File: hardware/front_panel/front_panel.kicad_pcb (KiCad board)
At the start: 2 copper layers, 60 x 40 mm, 4 parts

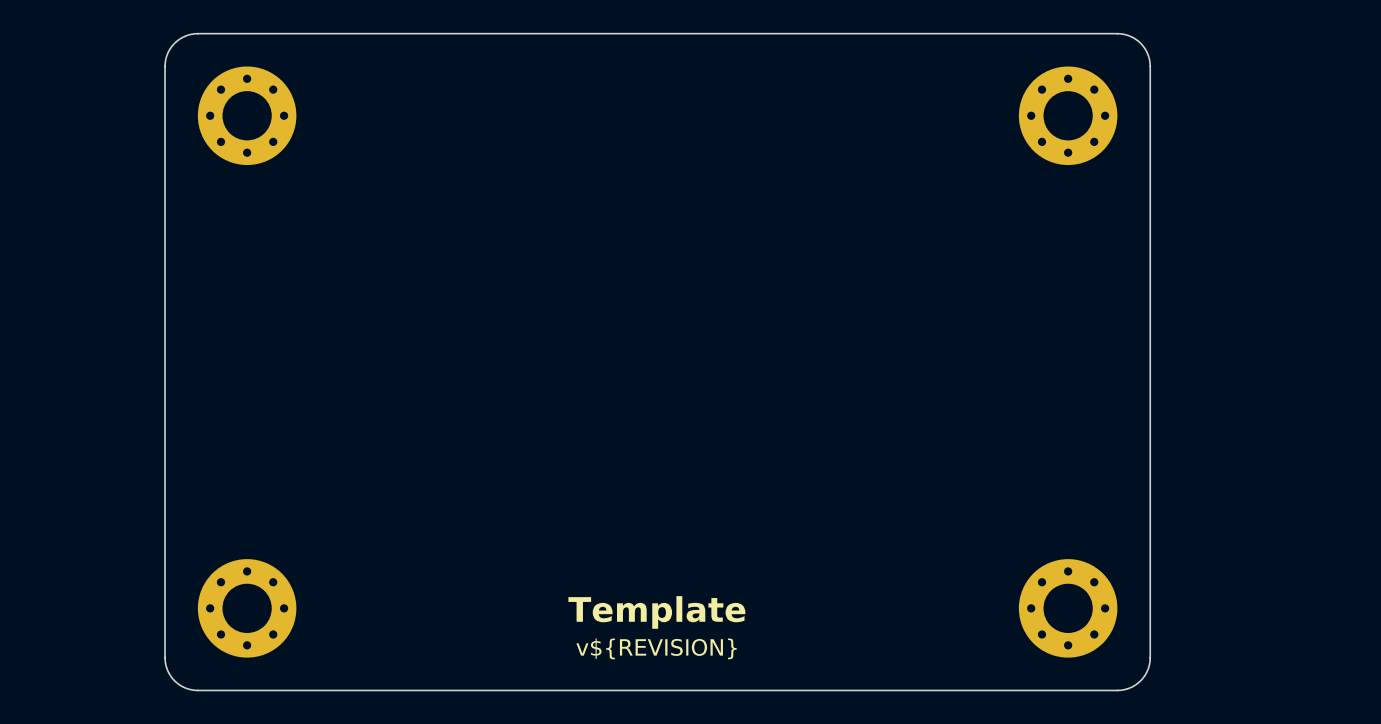
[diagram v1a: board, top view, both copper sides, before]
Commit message: Place components on the front panel PCB
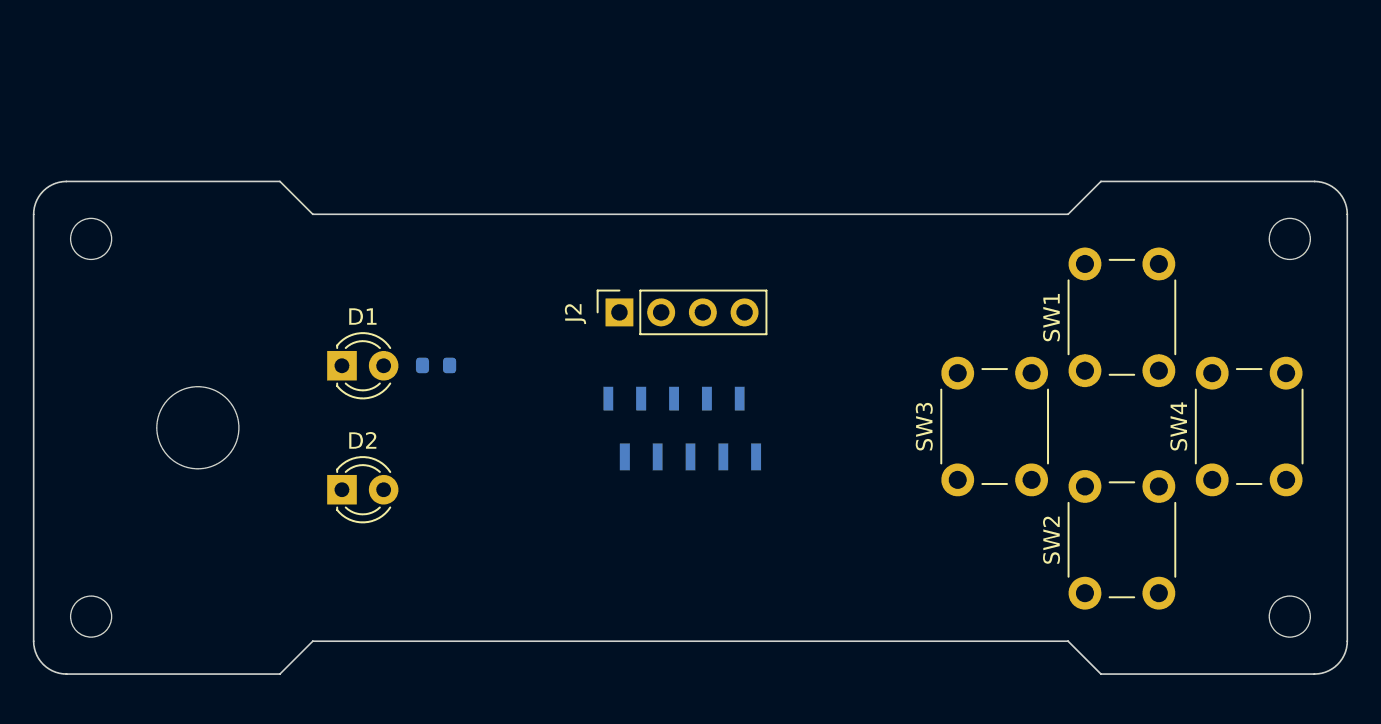
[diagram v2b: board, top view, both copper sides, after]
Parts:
- removed REF** (x4): MountingHole_3mm_Pad_Via, MountingHole:MountingHole_3mm_Pad_Via
- added D1: Green, LED_THT:LED_D3.0mm_FlatTop, F.Cu at (126.8, 96.2)
- added D2: Orange, LED_THT:LED_D3.0mm_FlatTop, F.Cu at (126.8, 103.8)
- added H1: 2.5mm, MountingHole:MountingHole_2.5mm, F.Cu at (111.5, 111.5)
- added H2: 2.5mm, MountingHole:MountingHole_2.5mm, F.Cu at (184.5, 111.5)
- added H3: 2.5mm, MountingHole:MountingHole_2.5mm, F.Cu at (184.5, 88.5)
- added H4: 2.5mm, MountingHole:MountingHole_2.5mm, F.Cu at (111.5, 88.5)
- added H5: 5mm, MountingHole:MountingHole_5mm, F.Cu at (118.0, 100.0)
- added J1: Panel, Local_Library:52808-1070, B.Cu at (147.5, 100.0)
- added J2: Display, Connector_PinSocket_2.54mm:PinSocket_1x04_P2.54mm_Vertical, F.Cu at (143.7, 93.0)
- added R1: 270R, Resistor_SMD:R_0603_1608Metric, B.Cu at (132.5, 96.2)
- added SW1: Up, Button_Switch_THT:SW_PUSH_6mm_H7.3mm, F.Cu at (172.0, 96.5)
- added SW2: Down, Button_Switch_THT:SW_PUSH_6mm_H7.3mm, F.Cu at (172.0, 110.1)
- added SW3: Left, Button_Switch_THT:SW_PUSH_6mm_H7.3mm, F.Cu at (164.3, 103.2)
- added SW4: Right, Button_Switch_THT:SW_PUSH_6mm_H7.3mm, F.Cu at (179.8, 103.2)
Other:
- board size 60 x 40 mm -> 80 x 30 mm
- board text added: "JLCJLCJLCJLC"
- board text removed: "Template"
- board text removed: "v${REVISION}"

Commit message: Route front panel PCB tracks
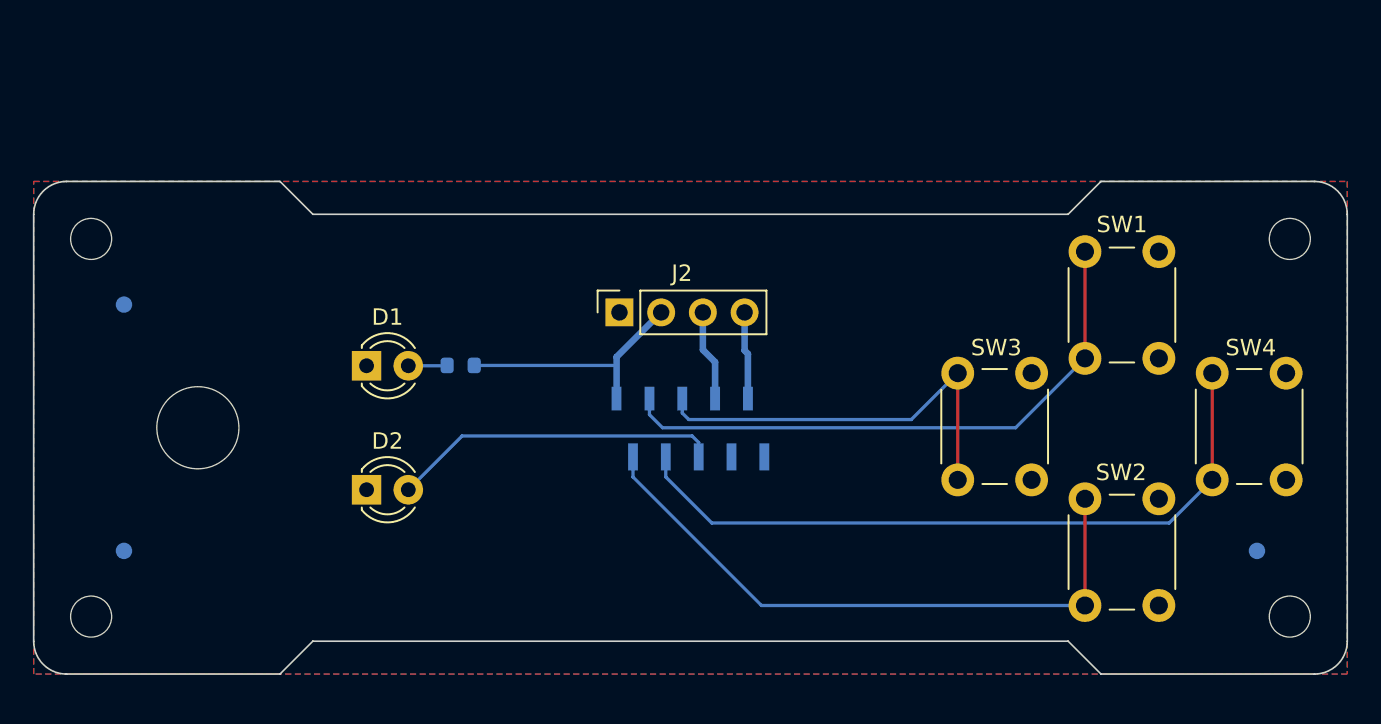
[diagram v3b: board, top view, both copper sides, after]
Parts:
- added FID1: Fiducial, Fiducial:Fiducial_1mm_Mask2mm, B.Cu at (113.5, 92.5)
- added FID2: Fiducial, Fiducial:Fiducial_1mm_Mask2mm, B.Cu at (113.5, 107.5)
- added FID3: Fiducial, Fiducial:Fiducial_1mm_Mask2mm, B.Cu at (182.5, 107.5)
- added REF**: WEEE-Logo_4.2x6mm_SilkScreen, Symbol:WEEE-Logo_4.2x6mm_SilkScreen, B.Cu at (120.0, 109.0)
- added REF**: OSHW-Logo2_7.3x6mm_SilkScreen, Symbol:OSHW-Logo2_7.3x6mm_SilkScreen, B.Cu at (120.0, 91.0)
- moved SW1 8.53 mm to (176.5, 89.3), turned to -90 degrees
- moved SW3 7.91 mm to (168.8, 96.7), turned to -90 degrees
- moved SW4 7.91 mm to (184.3, 96.7), turned to -90 degrees
- moved SW2 7.30 mm to (176.5, 104.3), turned to -90 degrees
- moved D1 1.50 mm to (128.3, 96.2)
- moved D2 1.50 mm to (128.3, 103.8)
- moved R1 1.50 mm to (134.0, 96.2)
- moved J1 0.50 mm to (148.0, 100.0)
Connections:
- D2 pad 2: Net-(D2-A) -> /STATUS
- J1 pad 1: GND -> +3.3V
- J1 pad 10: +3.3V -> GND
- J1 pad 2: /RIGHT -> /DOWN
- J1 pad 3: /LEFT -> /UP
- J1 pad 4: /DOWN -> /RIGHT
- J1 pad 5: /UP -> /LEFT
- J1 pad 7: GND -> /SCL
- J1 pad 8: /SDA -> GND
- J1 pad 9: /SCL -> /SDA
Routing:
- net /RIGHT: track 0.00 -> 43.2 mm
- net /DOWN: track 0.00 -> 38.5 mm
- net /UP: track 0.00 -> 36.1 mm
- net /LEFT: track 0.00 -> 25.5 mm
- net /STATUS: track 0.00 -> 20.1 mm
- net +3.3V: track 0.00 -> 15.0 mm
- net /SCL: track 0.00 -> 5.56 mm
- net /SDA: track 0.00 -> 5.33 mm
- net Net-(D1-A): track 0.00 -> 2.37 mm
- added copper zone on B.Cu, net GND
- added copper zone on F.Cu, net GND
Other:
- board text added: "Front Panel"
- board text added: "v${REVISION}"

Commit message: Route control board PCB tracks
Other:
- board text added: "20230904"
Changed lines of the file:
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@@
   (title_block
     (title "Reflow Hot Plate Front Panel")
-    (date "2023-08-09")
+    (date "2023-09-04")
     (rev "${REVISION}")
     (company "Author: I. Kajdan")
@@
     (pad_to_mask_clearance 0.05)
     (aux_axis_origin 108 115)
+    (grid_origin 108 115)
     (pcbplotparams
       (layerselection 0x00010fc_ffffffff)
@@
     )
   )
-  (footprint "MountingHole:MountingHole_2.5mm" (layer "F.Cu")
+  (footprint "MountingHole:MountingHole_2.5mm" locked (layer "F.Cu")
     (at 111.5 88.5)
     (descr "Mounting Hole 2.5mm, no annular")
@@
     (fp_circle (center 0 0) (end 2.75 0)
       (stroke (width 0.05) (type solid)) (fill none) (layer "F.CrtYd"))
-    (pad "" np_thru_hole circle (at 0 0) (size 2.5 2.5) (drill 2.5) (layers "*.Cu" "*.Mask"))
+    (pad "" np_thru_hole circle locked (at 0 0) (size 2.5 2.5) (drill 2.5) (layers "*.Cu" "*.Mask"))
   )
   (footprint "Connector_PinSocket_2.54mm:PinSocket_1x04_P2.54mm_Vertical" (layer "F.Cu")
@@
     )
   )
-  (footprint "MountingHole:MountingHole_2.5mm" (layer "F.Cu")
+  (footprint "MountingHole:MountingHole_2.5mm" locked (layer "F.Cu")
     (at 111.5 111.5)
     (descr "Mounting Hole 2.5mm, no annular")
@@
     (fp_circle (center 0 0) (end 2.75 0)
       (stroke (width 0.05) (type solid)) (fill none) (layer "F.CrtYd"))
-    (pad "" np_thru_hole circle (at 0 0) (size 2.5 2.5) (drill 2.5) (layers "*.Cu" "*.Mask"))
+    (pad "" np_thru_hole circle locked (at 0 0) (size 2.5 2.5) (drill 2.5) (layers "*.Cu" "*.Mask"))
   )
   (footprint "MountingHole:MountingHole_5mm" (layer "F.Cu")
@@
     (pad "" np_thru_hole circle (at 0 0) (size 5 5) (drill 5) (layers "*.Cu" "*.Mask"))
   )
-  (footprint "MountingHole:MountingHole_2.5mm" (layer "F.Cu")
+  (footprint "MountingHole:MountingHole_2.5mm" locked (layer "F.Cu")
     (at 184.5 111.5)
     (descr "Mounting Hole 2.5mm, no annular")
@@
     (fp_circle (center 0 0) (end 2.75 0)
       (stroke (width 0.05) (type solid)) (fill none) (layer "F.CrtYd"))
-    (pad "" np_thru_hole circle (at 0 0) (size 2.5 2.5) (drill 2.5) (layers "*.Cu" "*.Mask"))
+    (pad "" np_thru_hole circle locked (at 0 0) (size 2.5 2.5) (drill 2.5) (layers "*.Cu" "*.Mask"))
   )
-  (footprint "MountingHole:MountingHole_2.5mm" (layer "F.Cu")
+  (footprint "MountingHole:MountingHole_2.5mm" locked (layer "F.Cu")
     (at 184.5 88.5)
     (descr "Mounting Hole 2.5mm, no annular")
@@
     (fp_circle (center 0 0) (end 2.75 0)
       (stroke (width 0.05) (type solid)) (fill none) (layer "F.CrtYd"))
-    (pad "" np_thru_hole circle (at 0 0) (size 2.5 2.5) (drill 2.5) (layers "*.Cu" "*.Mask"))
+    (pad "" np_thru_hole circle locked (at 0 0) (size 2.5 2.5) (drill 2.5) (layers "*.Cu" "*.Mask"))
   )
   (footprint "Local_Library:52808-1070" (layer "B.Cu")
@@
       (solder_mask_margin 0.5) (clearance 0.5))
   )
-  (gr_line (start 188 87) (end 188 113)
+  (gr_line locked (start 188 87) (end 188 113)
     (stroke (width 0.1) (type default)) (layer "Edge.Cuts"))
-  (gr_arc (start 186 85) (mid 187.414214 85.585786) (end 188 87)
+  (gr_arc locked (start 186 85) (mid 187.414214 85.585786) (end 188 87)
     (stroke (width 0.1) (type default)) (layer "Edge.Cuts"))
-  (gr_line (start 171 87) (end 125 87)
+  (gr_line locked (start 171 87) (end 125 87)
     (stroke (width 0.1) (type default)) (layer "Edge.Cuts"))
-  (gr_line (start 125 113) (end 123 115)
+  (gr_line locked (start 125 113) (end 123 115)
     (stroke (width 0.1) (type default)) (layer "Edge.Cuts"))
-  (gr_line (start 125 87) (end 123 85)
+  (gr_line locked (start 125 87) (end 123 85)
     (stroke (width 0.1) (type default)) (layer "Edge.Cuts"))
-  (gr_arc (start 108 87) (mid 108.585786 85.585786) (end 110 85)
+  (gr_arc locked (start 108 87) (mid 108.585786 85.585786) (end 110 85)
     (stroke (width 0.1) (type default)) (layer "Edge.Cuts"))
-  (gr_line (start 186 115) (end 173 115)
+  (gr_line locked (start 186 115) (end 173 115)
     (stroke (width 0.1) (type default)) (layer "Edge.Cuts"))
-  (gr_line (start 108 113) (end 108 87)
+  (gr_line locked (start 108 113) (end 108 87)
     (stroke (width 0.1) (type default)) (layer "Edge.Cuts"))
-  (gr_arc (start 110 115) (mid 108.585786 114.414214) (end 108 113)
+  (gr_arc locked (start 110 115) (mid 108.585786 114.414214) (end 108 113)
     (stroke (width 0.1) (type default)) (layer "Edge.Cuts"))
-  (gr_line (start 173 85) (end 186 85)
+  (gr_line locked (start 173 85) (end 186 85)
     (stroke (width 0.1) (type default)) (layer "Edge.Cuts"))
-  (gr_line (start 110 85) (end 123 85)
+  (gr_line locked (start 110 85) (end 123 85)
     (stroke (width 0.1) (type default)) (layer "Edge.Cuts"))
-  (gr_line (start 173 115) (end 171 113)
+  (gr_line locked (start 173 115) (end 171 113)
     (stroke (width 0.1) (type default)) (layer "Edge.Cuts"))
-  (gr_line (start 123 115) (end 110 115)
+  (gr_line locked (start 123 115) (end 110 115)
     (stroke (width 0.1) (type default)) (layer "Edge.Cuts"))
-  (gr_line (start 171 113) (end 125 113)
+  (gr_line locked (start 171 113) (end 125 113)
     (stroke (width 0.1) (type default)) (layer "Edge.Cuts"))
-  (gr_line (start 171 87) (end 173 85)
+  (gr_line locked (start 171 87) (end 173 85)
     (stroke (width 0.1) (type default)) (layer "Edge.Cuts"))
-  (gr_arc (start 188 113) (mid 187.414214 114.414214) (end 186 115)
+  (gr_arc locked (start 188 113) (mid 187.414214 114.414214) (end 186 115)
     (stroke (width 0.1) (type default)) (layer "Edge.Cuts"))
   (gr_text "Front Panel" (at 148 108) (layer "B.SilkS")
     (effects (font (size 1.7 1.7) (thickness 0.3) bold) (justify bottom mirror))
   )
+  (gr_text "20230904" (at 147.5 89.5) (layer "B.SilkS")
+    (effects (font (size 1 1) (thickness 0.15)) (justify mirror))
+  )
   (gr_text "JLCJLCJLCJLC" (at 109.5 100.1 90) (layer "B.SilkS")

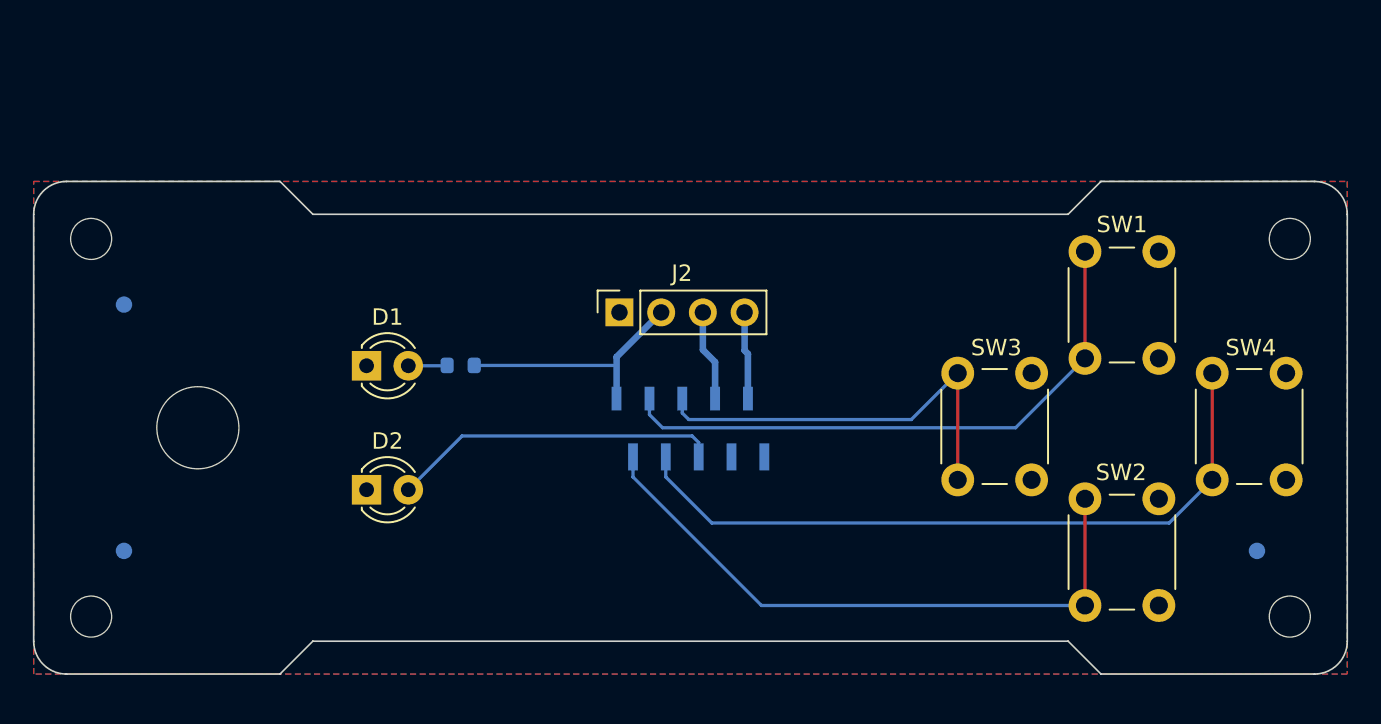
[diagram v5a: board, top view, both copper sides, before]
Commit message: Stitch the ground planes
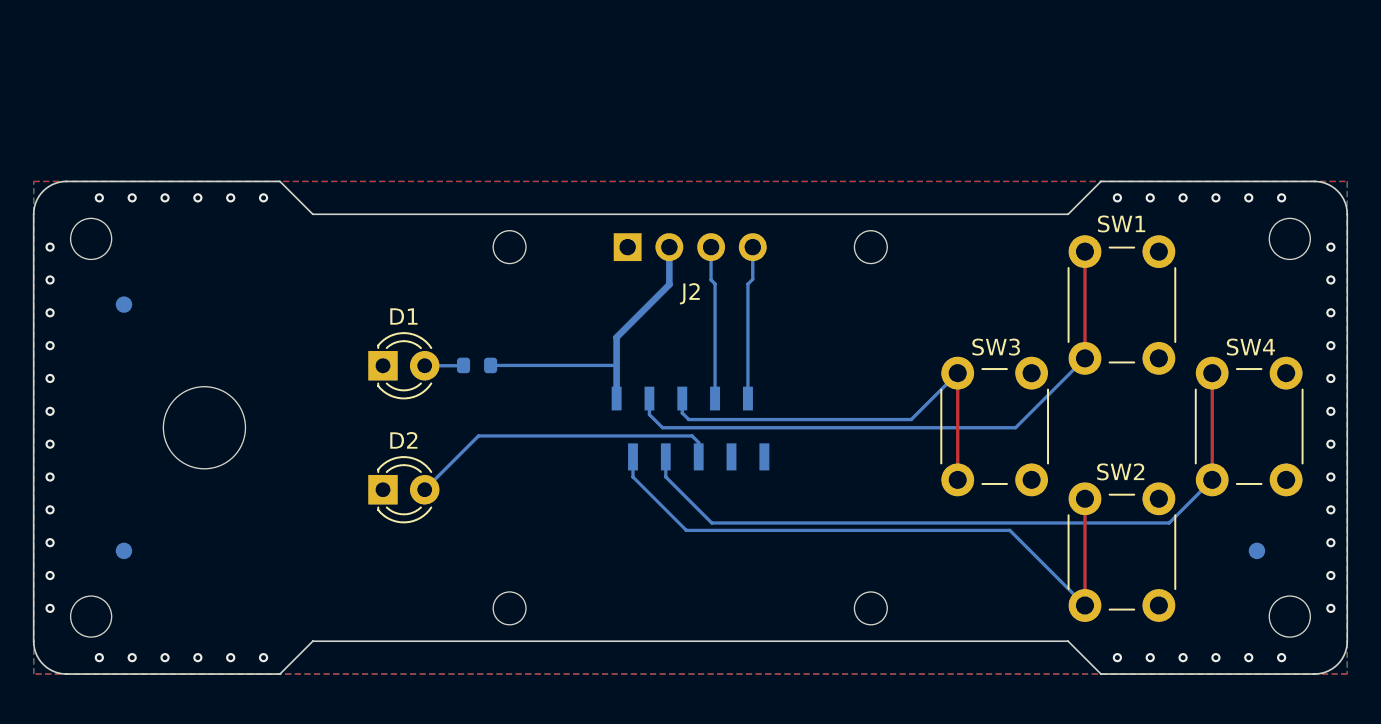
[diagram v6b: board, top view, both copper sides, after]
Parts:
- J2: footprint Connector_PinSocket_2.54mm:PinSocket_1x04_P2.54mm_Vertical -> Local_Library:0.96_OLED
- moved J2 4.01 mm to (144.2, 89.0), turned to 0 degrees
- moved D1 1.00 mm to (129.3, 96.2)
- moved D2 1.00 mm to (129.3, 103.8)
- moved R1 1.00 mm to (135.0, 96.2)
- moved H5 0.40 mm to (118.4, 100.0)
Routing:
- net /SDA: track 5.33 -> 9.35 mm
- net /SCL: track 5.56 -> 9.36 mm
- net +3.3V: track 15.0 -> 18.2 mm
- net /STATUS: track 20.1 -> 19.1 mm
- net GND: vias 0 -> 48
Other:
- board text added: "20230911"
- board text removed: "20230904"
